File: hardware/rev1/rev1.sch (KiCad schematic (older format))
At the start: 28 parts, among them U1 BNO055, U2 MPL3115A2, U3 Teensy3.6, Y1 Crystal_32kHz768

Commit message: wip
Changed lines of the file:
@@
 Text GLabel 27400 4300 0    50   Input ~ 0
 INT2_MPL3115A2
+Text GLabel 27400 3400 0    50   Input ~ 0
+nRESET
 Text GLabel 27400 3500 0    50   Input ~ 0
-nRESET
-Text GLabel 27400 3400 0    50   Input ~ 0
 INT_BNO055
 Text GLabel 27400 3100 0    50   Input ~ 0

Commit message: (mostly) fix electrical rules check
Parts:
- TP1, TP10, TP2, TP3, TP4, TP5, TP6, TP7, TP8, TP9, TP_GND1: footprint footprints:Test_Point_D1.02mm -> footprints:Test-Point-Pin_Drill2.79mm
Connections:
- wire segments 144 -> 138
- no-connect marks 0 -> 76
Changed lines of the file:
@@
 VDDIO
-$Comp
-L power:PWR_FLAG #FLG0101
-U 1 1 60279C57
-P 19750 2750
-F 0 "#FLG0101" H 19750 2825 50  0001 C CNN
-F 1 "PWR_FLAG" H 19750 2923 50  0000 C CNN
-F 2 "" H 19750 2750 50  0001 C CNN
-F 3 "~" H 19750 2750 50  0001 C CNN
-	1    19750 2750
-	1    0    0    -1
-$EndComp
 $Comp
 L power:GNDPWR #PWR0101
@@
 $EndComp
 Wire Wire Line
-	19750 3100 19750 3000
-Wire Wire Line
-	19750 3000 20150 3000
-Wire Wire Line
 	20150 3000 20150 3100
 Wire Wire Line
 	20150 2750 20150 2850
-Wire Wire Line
-	20150 2850 19750 2850
-Wire Wire Line
-	19750 2850 19750 2750
 $Comp
 L Connector:TestPoint TP8
@@
 F 0 "TP8" H 17658 1968 50  0000 L CNN
 F 1 "TestPoint" H 17658 1877 50  0000 L CNN
-F 2 "footprints:Test_Point_D1.02mm" H 17800 1850 50  0001 C CNN
+F 2 "footprints:Test-Point-Pin_Drill2.79mm" H 17800 1850 50  0001 C CNN
 F 3 "~" H 17800 1850 50  0001 C CNN
 	1    17600 1850
@@
 Text GLabel 20550 2750 1    50   Input ~ 0
 VDDIO
-Connection ~ 20150 2850
 $Comp
 L Connector:TestPoint TP6
@@
 F 0 "TP6" H 21008 2968 50  0000 L CNN
 F 1 "TestPoint" H 21008 2877 50  0000 L CNN
-F 2 "footprints:Test_Point_D1.02mm" H 21150 2850 50  0001 C CNN
+F 2 "footprints:Test-Point-Pin_Drill2.79mm" H 21150 2850 50  0001 C CNN
 F 3 "~" H 21150 2850 50  0001 C CNN
 	1    20950 2850
@@
 F 0 "TP7" H 21008 3118 50  0000 L CNN
 F 1 "TestPoint" H 21008 3027 50  0000 L CNN
-F 2 "footprints:Test_Point_D1.02mm" H 21150 3000 50  0001 C CNN
+F 2 "footprints:Test-Point-Pin_Drill2.79mm" H 21150 3000 50  0001 C CNN
 F 3 "~" H 21150 3000 50  0001 C CNN
 	1    20950 3000
@@
 Wire Wire Line
 	20150 3000 20550 3000
-Connection ~ 20150 3000
 Wire Wire Line
 	20150 2850 20550 2850
@@
 Wire Wire Line
 	20550 3000 20950 3000
-$Comp
-L power:PWR_FLAG #FLG0106
-U 1 1 60279C66
-P 19750 3100
-F 0 "#FLG0106" H 19750 3175 50  0001 C CNN
-F 1 "PWR_FLAG" H 19750 3273 50  0000 C CNN
-F 2 "" H 19750 3100 50  0001 C CNN
-F 3 "~" H 19750 3100 50  0001 C CNN
-	1    19750 3100
-	-1   0    0    1
-$EndComp
 Text Notes 16300 1050 0    197  ~ 0
 Altimeter w/ Logic Shifter
@@
 F 0 "TP2" H 2792 5226 50  0000 R CNN
 F 1 "TestPoint" H 2792 5317 50  0000 R CNN
-F 2 "footprints:Test_Point_D1.02mm" H 3050 5200 50  0001 C CNN
+F 2 "footprints:Test-Point-Pin_Drill2.79mm" H 3050 5200 50  0001 C CNN
 F 3 "~" H 3050 5200 50  0001 C CNN
 	1    2850 5200
@@
 F 0 "TP3" H 5242 7926 50  0000 R CNN
 F 1 "TestPoint" H 5242 8017 50  0000 R CNN
-F 2 "footprints:Test_Point_D1.02mm" H 5500 7900 50  0001 C CNN
+F 2 "footprints:Test-Point-Pin_Drill2.79mm" H 5500 7900 50  0001 C CNN
 F 3 "~" H 5500 7900 50  0001 C CNN
 	1    5300 7900
@@
 F 0 "TP1" H 2642 7576 50  0000 R CNN
 F 1 "TestPoint" H 2642 7667 50  0000 R CNN
-F 2 "footprints:Test_Point_D1.02mm" H 2900 7550 50  0001 C CNN
+F 2 "footprints:Test-Point-Pin_Drill2.79mm" H 2900 7550 50  0001 C CNN
 F 3 "~" H 2900 7550 50  0001 C CNN
 	1    2700 7550
@@
 F 0 "TP_GND1" H 6592 6976 50  0000 R CNN
 F 1 "TestPoint" H 6592 7067 50  0000 R CNN
-F 2 "footprints:Test_Point_D1.02mm" H 6850 6950 50  0001 C CNN
+F 2 "footprints:Test-Point-Pin_Drill2.79mm" H 6850 6950 50  0001 C CNN
 F 3 "~" H 6850 6950 50  0001 C CNN
 	1    6650 6950
@@
 Wire Wire Line
 	9250 5400 9250 5950
-Wire Wire Line
-	3150 2750 3150 2450
-Connection ~ 3150 2750
-$Comp
-L power:PWR_FLAG #FLG0102
-U 1 1 5F8BCADC
-P 3150 2750
-F 0 "#FLG0102" H 3150 2825 50  0001 C CNN
-F 1 "PWR_FLAG" V 3150 2877 50  0000 L CNN
-F 2 "" H 3150 2750 50  0001 C CNN
-F 3 "~" H 3150 2750 50  0001 C CNN
-	1    3150 2750
-	0    -1   -1   0
-$EndComp
-Wire Wire Line
-	2050 2750 2050 2450
-Connection ~ 2050 2750
-$Comp
-L power:PWR_FLAG #FLG0107
-U 1 1 5F8BC0A5
-P 2050 2750
-F 0 "#FLG0107" H 2050 2825 50  0001 C CNN
-F 1 "PWR_FLAG" V 2050 2877 50  0000 L CNN
-F 2 "" H 2050 2750 50  0001 C CNN
-F 3 "~" H 2050 2750 50  0001 C CNN
-	1    2050 2750
-	0    -1   -1   0
-$EndComp
 Wire Wire Line
 	2050 2450 2050 2350
@@
 Wire Wire Line
 	3150 4950 3150 3500
-Wire Wire Line
-	3150 3500 3150 2750
 Connection ~ 3800 4700
 Wire Wire Line
@@
 	2050 7550 2050 6700
 Wire Wire Line
-	2050 2950 2050 2750
-Wire Wire Line
 	3800 4700 3800 5450
 $Comp
@@
 F 0 "TP5" H 3792 8576 50  0000 R CNN
 F 1 "TestPoint" H 3792 8667 50  0000 R CNN
-F 2 "footprints:Test_Point_D1.02mm" H 4050 8550 50  0001 C CNN
+F 2 "footprints:Test-Point-Pin_Drill2.79mm" H 4050 8550 50  0001 C CNN
 F 3 "~" H 4050 8550 50  0001 C CNN
 	1    3850 8550
@@
 F 0 "TP4" H 1792 8276 50  0000 R CNN
 F 1 "TestPoint" H 1792 8367 50  0000 R CNN
-F 2 "footprints:Test_Point_D1.02mm" H 2050 8250 50  0001 C CNN
+F 2 "footprints:Test-Point-Pin_Drill2.79mm" H 2050 8250 50  0001 C CNN
 F 3 "~" H 2050 8250 50  0001 C CNN
 	1    1850 8250
@@
 F 0 "TP10" H 11342 2526 50  0000 R CNN
 F 1 "TestPoint" H 11342 2617 50  0000 R CNN
-F 2 "footprints:Test_Point_D1.02mm" H 11600 2500 50  0001 C CNN
+F 2 "footprints:Test-Point-Pin_Drill2.79mm" H 11600 2500 50  0001 C CNN
 F 3 "~" H 11600 2500 50  0001 C CNN
 	1    11400 2500
@@
 F 0 "TP9" H 11342 1826 50  0000 R CNN
 F 1 "TestPoint" H 11342 1917 50  0000 R CNN
-F 2 "footprints:Test_Point_D1.02mm" H 11600 1800 50  0001 C CNN
+F 2 "footprints:Test-Point-Pin_Drill2.79mm" H 11600 1800 50  0001 C CNN
 F 3 "~" H 11600 1800 50  0001 C CNN
 	1    11400 1800
@@
 Text GLabel 27400 3700 0    39   Input ~ 0
 SDA_TEENSY
+NoConn ~ 27400 2900
+NoConn ~ 27400 3000
+NoConn ~ 27400 3200
+NoConn ~ 27400 3300
+NoConn ~ 27400 3800
+NoConn ~ 27400 3900
+NoConn ~ 27400 4100
+NoConn ~ 27400 4500
+NoConn ~ 27400 4600
+NoConn ~ 27400 4700
+NoConn ~ 27400 4800
+NoConn ~ 27400 4900
+NoConn ~ 27400 5000
+NoConn ~ 27400 5100
+NoConn ~ 27400 5200
+NoConn ~ 27400 5300
+NoConn ~ 27400 5400
+NoConn ~ 27400 5500
+NoConn ~ 27400 5600
+NoConn ~ 27400 5700
+NoConn ~ 27400 5800
+NoConn ~ 27400 5900
+NoConn ~ 27400 6000
+NoConn ~ 27400 6100
+NoConn ~ 27400 6200
+NoConn ~ 27400 6300
+NoConn ~ 27400 6400
+NoConn ~ 27400 6500
+NoConn ~ 27400 6600
+NoConn ~ 27400 6700
+NoConn ~ 27400 6800
+NoConn ~ 27400 6900
+NoConn ~ 27400 7000
+NoConn ~ 27400 7100
+NoConn ~ 29700 7100
+NoConn ~ 29700 7000
+NoConn ~ 29700 6900
+NoConn ~ 29700 6800
+NoConn ~ 29700 6700
+NoConn ~ 29700 6600
+NoConn ~ 29700 6500
+NoConn ~ 29700 6400
+NoConn ~ 29700 6300
+NoConn ~ 29700 6200
+NoConn ~ 29700 6100
+NoConn ~ 29700 6000
+NoConn ~ 29700 5900
+NoConn ~ 29700 5600
+NoConn ~ 29700 5500
+NoConn ~ 29700 5400
+NoConn ~ 29700 5300
+NoConn ~ 29700 5200
+NoConn ~ 29700 5100
+NoConn ~ 29700 5000
+NoConn ~ 29700 4900
+NoConn ~ 29700 4800
+NoConn ~ 29700 4700
+NoConn ~ 29700 4600
+NoConn ~ 29700 4500
+NoConn ~ 29700 4400
+NoConn ~ 29700 4300
+NoConn ~ 29700 4200
+NoConn ~ 29700 4100
+NoConn ~ 29700 4000
+NoConn ~ 29700 3900
+NoConn ~ 29700 3800
+NoConn ~ 29700 3700
+NoConn ~ 29700 3600
+NoConn ~ 29700 3500
+NoConn ~ 29700 3400
+NoConn ~ 29700 3300
+NoConn ~ 29700 3200
+NoConn ~ 29700 3100
+NoConn ~ 29700 3000
+NoConn ~ 29700 2900
+NoConn ~ 29700 2800
+Wire Wire Line
+	3150 2450 3150 3500
+Wire Wire Line
+	2050 2450 2050 2950
 $EndSCHEMATC

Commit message: label test points
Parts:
- removed TP_GND1: TestPoint, footprints:Test-Point-Pin_Drill2.79mm, symbol Connector:TestPoint
- renumbered TP2 to BOOT1, TP3 to CAP1, TP8 to CAP2, TP4 to GND1, TP7 to GND2, TP9 to OSCin1, TP10 to OSCout1, TP5 to VDD1, TP6 to VDD2, TP1 to nReset1
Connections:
- wire segments 138 -> 133
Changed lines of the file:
@@
 	20150 2750 20150 2850
 $Comp
-L Connector:TestPoint TP8
+L Connector:TestPoint CAP2
 U 1 1 5FEA9553
 P 17600 1850
-F 0 "TP8" H 17658 1968 50  0000 L CNN
+F 0 "CAP2" H 17658 1968 50  0000 L CNN
 F 1 "TestPoint" H 17658 1877 50  0000 L CNN
 F 2 "footprints:Test-Point-Pin_Drill2.79mm" H 17800 1850 50  0001 C CNN
@@
 VDDIO
 $Comp
-L Connector:TestPoint TP6
+L Connector:TestPoint VDD2
 U 1 1 60279C64
 P 20950 2850
-F 0 "TP6" H 21008 2968 50  0000 L CNN
+F 0 "VDD2" H 21008 2968 50  0000 L CNN
 F 1 "TestPoint" H 21008 2877 50  0000 L CNN
 F 2 "footprints:Test-Point-Pin_Drill2.79mm" H 21150 2850 50  0001 C CNN
@@
 $EndComp
 $Comp
-L Connector:TestPoint TP7
+L Connector:TestPoint GND2
 U 1 1 60279C65
 P 20950 3000
-F 0 "TP7" H 21008 3118 50  0000 L CNN
+F 0 "GND2" H 21008 3118 50  0000 L CNN
 F 1 "TestPoint" H 21008 3027 50  0000 L CNN
 F 2 "footprints:Test-Point-Pin_Drill2.79mm" H 21150 3000 50  0001 C CNN
@@
 	2850 5200 2500 5200
 Connection ~ 2850 5200
-$Comp
-L Connector:TestPoint TP2
-U 1 1 5FEF6DE2
-P 2850 5200
-F 0 "TP2" H 2792 5226 50  0000 R CNN
-F 1 "TestPoint" H 2792 5317 50  0000 R CNN
-F 2 "footprints:Test-Point-Pin_Drill2.79mm" H 3050 5200 50  0001 C CNN
-F 3 "~" H 3050 5200 50  0001 C CNN
-	1    2850 5200
-	-1   0    0    1
-$EndComp
 Wire Wire Line
 	3500 8400 3300 8400
@@
 Wire Wire Line
 	2950 8400 2950 8550
-Wire Wire Line
-	3850 8250 3850 8400
 $Comp
 L power:GND #PWR0106
@@
 	1    0    0    -1
 $EndComp
-$Comp
-L power:PWR_FLAG #FLG0105
-U 1 1 5FED08AB
-P 3850 8250
-F 0 "#FLG0105" H 3850 8325 50  0001 C CNN
-F 1 "PWR_FLAG" H 3850 8423 50  0000 C CNN
-F 2 "" H 3850 8250 50  0001 C CNN
-F 3 "~" H 3850 8250 50  0001 C CNN
-	1    3850 8250
-	1    0    0    -1
-$EndComp
-Connection ~ 1400 8450
 Wire Wire Line
 	1850 8450 1850 8550
@@
 Wire Wire Line
 	1400 8450 1400 8550
-Wire Wire Line
-	950  8450 1400 8450
-Wire Wire Line
-	950  8550 950  8450
-$Comp
-L power:PWR_FLAG #FLG0104
-U 1 1 5FEC6EA1
-P 950 8550
-F 0 "#FLG0104" H 950 8625 50  0001 C CNN
-F 1 "PWR_FLAG" H 950 8723 50  0000 C CNN
-F 2 "" H 950 8550 50  0001 C CNN
-F 3 "~" H 950 8550 50  0001 C CNN
-	1    950  8550
-	-1   0    0    1
-$EndComp
 $Comp
 L power:GNDPWR #PWR0108
@@
 Wire Wire Line
 	5300 7900 5300 6250
-$Comp
-L Connector:TestPoint TP3
-U 1 1 5FEC0903
-P 5300 7900
-F 0 "TP3" H 5242 7926 50  0000 R CNN
-F 1 "TestPoint" H 5242 8017 50  0000 R CNN
-F 2 "footprints:Test-Point-Pin_Drill2.79mm" H 5500 7900 50  0001 C CNN
-F 3 "~" H 5500 7900 50  0001 C CNN
-	1    5300 7900
-	-1   0    0    1
-$EndComp
 Wire Wire Line
 	2700 7550 6150 7550
 Connection ~ 2700 7550
 $Comp
-L Connector:TestPoint TP1
+L Connector:TestPoint nReset1
 U 1 1 5FEBC857
 P 2700 7550
-F 0 "TP1" H 2642 7576 50  0000 R CNN
+F 0 "nReset1" H 2642 7576 50  0000 R CNN
 F 1 "TestPoint" H 2642 7667 50  0000 R CNN
 F 2 "footprints:Test-Point-Pin_Drill2.79mm" H 2900 7550 50  0001 C CNN
 F 3 "~" H 2900 7550 50  0001 C CNN
 	1    2700 7550
-	-1   0    0    1
-$EndComp
-Wire Wire Line
-	6650 6950 6450 6950
-Connection ~ 6650 6950
-$Comp
-L Connector:TestPoint TP_GND1
-U 1 1 5FEAB6FE
-P 6650 6950
-F 0 "TP_GND1" H 6592 6976 50  0000 R CNN
-F 1 "TestPoint" H 6592 7067 50  0000 R CNN
-F 2 "footprints:Test-Point-Pin_Drill2.79mm" H 6850 6950 50  0001 C CNN
-F 3 "~" H 6850 6950 50  0001 C CNN
-	1    6650 6950
 	-1   0    0    1
 $EndComp
@@
 	1    0    0    -1
 $EndComp
-Connection ~ 9250 5950
-$Comp
-L power:PWR_FLAG #FLG0103
-U 1 1 5F8C2065
-P 9250 5950
-F 0 "#FLG0103" H 9250 6025 50  0001 C CNN
-F 1 "PWR_FLAG" V 9250 6077 50  0000 L CNN
-F 2 "" H 9250 5950 50  0001 C CNN
-F 3 "~" H 9250 5950 50  0001 C CNN
-	1    9250 5950
-	0    -1   -1   0
-$EndComp
-Wire Wire Line
-	9250 5400 9250 5950
 Wire Wire Line
 	2050 2450 2050 2350
@@
 Wire Wire Line
 	6450 6950 5900 6950
-Wire Wire Line
-	7150 6950 6650 6950
 $Comp
 L power:GND #PWR0109
@@
 $EndComp
 $Comp
-L Connector:TestPoint TP5
+L Connector:TestPoint VDD1
 U 1 1 5FF680D8
 P 3850 8550
-F 0 "TP5" H 3792 8576 50  0000 R CNN
+F 0 "VDD1" H 3792 8576 50  0000 R CNN
 F 1 "TestPoint" H 3792 8667 50  0000 R CNN
 F 2 "footprints:Test-Point-Pin_Drill2.79mm" H 4050 8550 50  0001 C CNN
@@
 $EndComp
 $Comp
-L Connector:TestPoint TP4
+L Connector:TestPoint GND1
 U 1 1 5FF68D98
 P 1850 8250
-F 0 "TP4" H 1792 8276 50  0000 R CNN
+F 0 "GND1" H 1792 8276 50  0000 R CNN
 F 1 "TestPoint" H 1792 8367 50  0000 R CNN
 F 2 "footprints:Test-Point-Pin_Drill2.79mm" H 2050 8250 50  0001 C CNN
@@
 	3850 8550 3850 8400
 Connection ~ 3850 8400
-Wire Wire Line
-	9250 5950 9250 6950
 $Comp
 L rev1-rescue:BNO055_BNO055-bno055 U1
@@
 Text GLabel 27400 4200 0    39   Input ~ 0
 VIN_TEENSY
-Wire Wire Line
-	6900 7300 9850 7300
 Text GLabel 9850 7300 2    50   Input ~ 0
 INT_BNO055
@@
 https://cdn-shop.adafruit.com/datasheets/BST_BNO055_DS000_12.pdf
 $Comp
-L Connector:TestPoint TP10
+L Connector:TestPoint OSCout1
 U 1 1 600A3D96
 P 11400 2500
-F 0 "TP10" H 11342 2526 50  0000 R CNN
+F 0 "OSCout1" H 11342 2526 50  0000 R CNN
 F 1 "TestPoint" H 11342 2617 50  0000 R CNN
 F 2 "footprints:Test-Point-Pin_Drill2.79mm" H 11600 2500 50  0001 C CNN
@@
 	11400 2500 10900 2500
 $Comp
-L Connector:TestPoint TP9
+L Connector:TestPoint OSCin1
 U 1 1 600A5053
 P 11400 1800
-F 0 "TP9" H 11342 1826 50  0000 R CNN
+F 0 "OSCin1" H 11342 1826 50  0000 R CNN
 F 1 "TestPoint" H 11342 1917 50  0000 R CNN
 F 2 "footprints:Test-Point-Pin_Drill2.79mm" H 11600 1800 50  0001 C CNN
@@
 Wire Wire Line
 	2050 2450 2050 2950
+Wire Wire Line
+	6450 6950 7150 6950
+Wire Wire Line
+	9250 5400 9250 6950
+$Comp
+L Connector:TestPoint CAP1
+U 1 1 5FEC0903
+P 5300 7900
+F 0 "CAP1" H 5242 7926 50  0000 R CNN
+F 1 "TestPoint" H 5242 8017 50  0000 R CNN
+F 2 "footprints:Test-Point-Pin_Drill2.79mm" H 5500 7900 50  0001 C CNN
+F 3 "~" H 5500 7900 50  0001 C CNN
+	1    5300 7900
+	-1   0    0    1
+$EndComp
+$Comp
+L Connector:TestPoint BOOT1
+U 1 1 5FEF6DE2
+P 2850 5200
+F 0 "BOOT1" H 2792 5226 50  0000 R CNN
+F 1 "TestPoint" H 2792 5317 50  0000 R CNN
+F 2 "footprints:Test-Point-Pin_Drill2.79mm" H 3050 5200 50  0001 C CNN
+F 3 "~" H 3050 5200 50  0001 C CNN
+	1    2850 5200
+	-1   0    0    1
+$EndComp
+Wire Wire Line
+	6900 7300 9850 7300
 $EndSCHEMATC

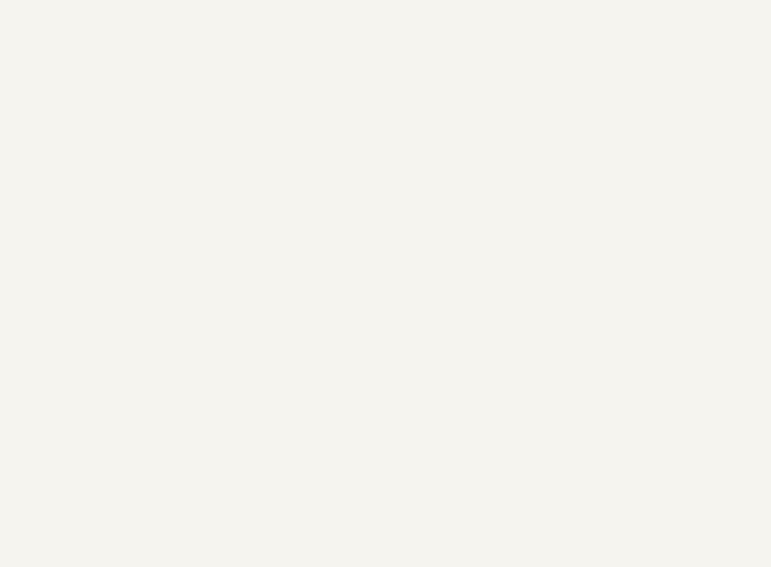
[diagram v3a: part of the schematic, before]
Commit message: add 2-pin header for BMS connection
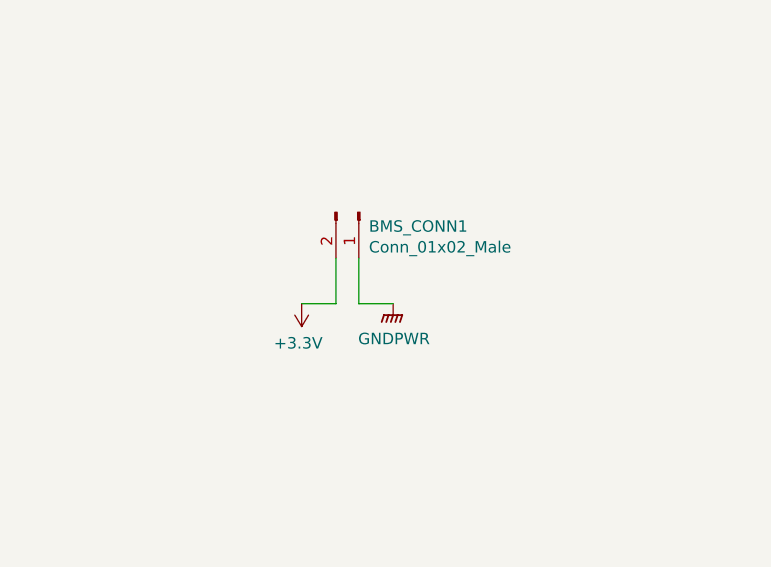
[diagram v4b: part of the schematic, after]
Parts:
- added BMS_CONN1: Conn_01x02_Male, Connector_PinHeader_2.54mm:PinHeader_1x02_P2.54mm_Vertical, symbol Connector:Conn_01x02_Male
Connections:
- net +3V3: now also BMS_CONN1.2 (Pin_2)
- net GND: now also BMS_CONN1.1 (Pin_1)
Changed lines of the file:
@@
 	16600 3050 17100 3050
-$Comp
-L power:+3.3V #PWR0103
-U 1 1 60279C5C
-P 20150 2750
-F 0 "#PWR0103" H 20150 2600 50  0001 C CNN
-F 1 "+3.3V" H 20165 2923 50  0000 C CNN
-F 2 "" H 20150 2750 50  0001 C CNN
-F 3 "" H 20150 2750 50  0001 C CNN
-	1    20150 2750
-	1    0    0    -1
-$EndComp
 $Comp
 L power:GND #PWR0104
@@
 NoConn ~ 29700 6500
 NoConn ~ 29700 6400
-NoConn ~ 29700 6300
 NoConn ~ 29700 6200
 NoConn ~ 29700 6100
@@
 Wire Wire Line
 	6900 7300 9850 7300
+$Comp
+L Connector:Conn_01x02_Male BMS_CONN1
+U 1 1 60257B5B
+P 28000 8900
+F 0 "BMS_CONN1" V 28062 8944 50  0000 L CNN
+F 1 "Conn_01x02_Male" V 28153 8944 50  0000 L CNN
+F 2 "Connector_PinHeader_2.54mm:PinHeader_1x02_P2.54mm_Vertical" H 28000 8900 50  0001 C CNN
+F 3 "~" H 28000 8900 50  0001 C CNN
+	1    28000 8900
+	0    1    1    0
+$EndComp
+$Comp
+L power:GNDPWR #PWR04
+U 1 1 6025A133
+P 28150 9300
+F 0 "#PWR04" H 28150 9100 50  0001 C CNN
+F 1 "GNDPWR" H 28154 9146 50  0000 C CNN
+F 2 "" H 28150 9250 50  0001 C CNN
+F 3 "" H 28150 9250 50  0001 C CNN
+	1    28150 9300
+	1    0    0    -1
+$EndComp
+$Comp
+L power:+3.3V #PWR0103
+U 1 1 60279C5C
+P 20150 2750
+F 0 "#PWR0103" H 20150 2600 50  0001 C CNN
+F 1 "+3.3V" H 20165 2923 50  0000 C CNN
+F 2 "" H 20150 2750 50  0001 C CNN
+F 3 "" H 20150 2750 50  0001 C CNN
+	1    20150 2750
+	1    0    0    -1
+$EndComp
+$Comp
+L power:+3.3V #PWR03
+U 1 1 6025DE3B
+P 27750 9300
+F 0 "#PWR03" H 27750 9150 50  0001 C CNN
+F 1 "+3.3V" H 27765 9473 50  0000 C CNN
+F 2 "" H 27750 9300 50  0001 C CNN
+F 3 "" H 27750 9300 50  0001 C CNN
+	1    27750 9300
+	-1   0    0    1
+$EndComp
+Wire Wire Line
+	27750 9300 27900 9300
+Wire Wire Line
+	27900 9300 27900 9100
+Wire Wire Line
+	28000 9100 28000 9300
+Wire Wire Line
+	28000 9300 28150 9300
+NoConn ~ 29700 6300
 $EndSCHEMATC
